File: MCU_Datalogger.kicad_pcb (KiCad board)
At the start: 2 copper layers, 29 parts, among them J1 Conn_01x04_Pin, J2 Conn_01x09_Pin, J3 Conn_01x04_Pin, J4 Conn_02x03_Odd_Even, U1 24LC1025, U2 DS1337S_, U3 24LC1025, U4 ATMEGA328P-AU, Y1 32.768 KHz, Y2 16MHz

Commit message: Completed placement of footprint
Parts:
- moved H3 71.4 mm to (180.7, 59.9)
- moved H4 62.7 mm to (180.7, 85.6)
- moved R7 58.2 mm to (167.8, 63.4)
- moved R5 57.8 mm to (172.3, 63.4)
- moved R6 57.6 mm to (172.3, 66.5)
- moved C5 55.7 mm to (163.0, 60.2)
- moved R4 50.5 mm to (167.7, 66.5)
- moved C3 48.5 mm to (158.4, 60.2)
- moved D2 47.5 mm to (167.7, 60.2)
- moved R3 47.3 mm to (167.8, 69.7), turned to 180 degrees
- moved D1 47.1 mm to (172.4, 60.2)
- moved BT1 46.4 mm to (136.7, 66.7)
- moved U4 42.0 mm to (157.4, 68.7)
- moved C1 41.4 mm to (153.9, 60.2)
- moved C4 40.8 mm to (167.7, 76.7)
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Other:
- board outline added: 50.8 x 30.5 mm

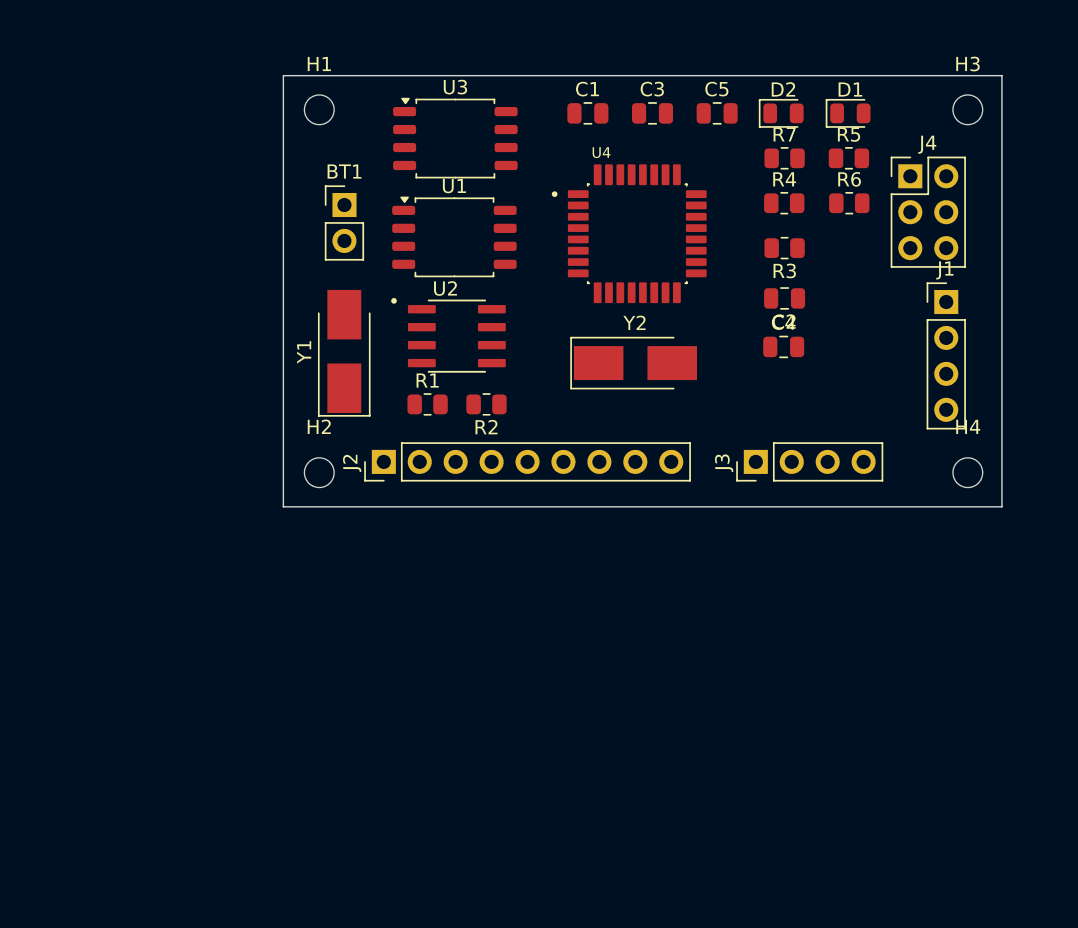
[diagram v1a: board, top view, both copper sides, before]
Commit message: Routing, GND Plane, Rework VCC Line and slick Screen complete
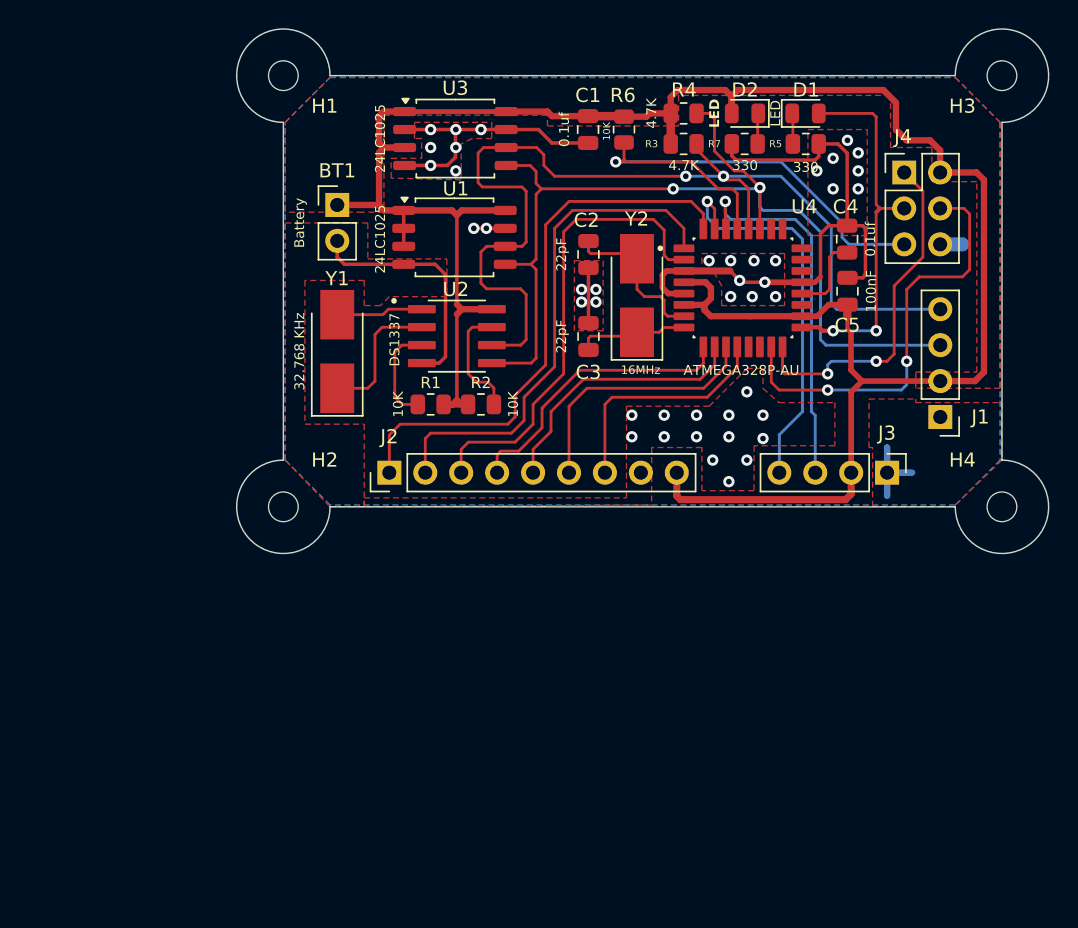
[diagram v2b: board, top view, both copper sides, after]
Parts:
- U2: value DS1337S_ -> DS1337
- moved R6 16.8 mm to (156.4, 61.3), turned to -90 degrees
- moved C3 16.4 mm to (153.9, 76.0), turned to -90 degrees
- moved C5 15.6 mm to (172.2, 72.8), turned to 90 degrees
- moved C2 14.2 mm to (153.9, 70.2), turned to 90 degrees
- moved R3 10.3 mm to (160.6, 62.4), turned to 0 degrees
- moved R4 9.53 mm to (160.6, 60.2)
- moved J3 9.31 mm to (175.0, 85.6), turned to -90 degrees
- moved C4 8.84 mm to (172.2, 69.1), turned to -90 degrees
- moved U4 8.40 mm to (164.8, 72.5)
- moved J1 8.14 mm to (178.8, 81.7), turned to 180 degrees
- moved Y2 4.78 mm to (157.3, 73.1), turned to 90 degrees
- moved H1 3.50 mm to (132.3, 57.5)
- moved H2 3.50 mm to (132.3, 88.0)
- moved H3 3.41 mm to (183.1, 57.5)
- moved H4 3.41 mm to (183.1, 88.0)
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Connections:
- BT1 pad 1: Net-(BT1-+) -> /Vcc
- C5 pad 1: Net-(BT1-+) -> /Vcc
- D1 pad 2: /SCL -> /SCK
- D2 pad 2: Net-(BT1-+) -> /Vcc
- J4 pad 3: /SCL -> /SCK
- U4 pad 17: /SCL -> /SCK
- U4 pad 18: Net-(BT1-+) -> /Vcc
- U4 pad 4: Net-(BT1-+) -> /Vcc
- U4 pad 6: Net-(BT1-+) -> /Vcc
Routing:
- net /Vcc: track 0.00 -> 163.0 mm
- net GND: track 0.00 -> 90.1 mm, vias 0 -> 43
- net /SCL: track 0.00 -> 73.6 mm, vias 0 -> 2
- net /SDA: track 0.00 -> 70.2 mm, vias 0 -> 2
- net /D2: track 0.00 -> 39.8 mm
- net /RESET: track 0.00 -> 36.8 mm, vias 0 -> 1
- net /D3: track 0.00 -> 36.0 mm
- net /D4: track 0.00 -> 33.0 mm
- net /MOSI: track 0.00 -> 30.4 mm, vias 0 -> 2
- net /TX: track 0.00 -> 27.9 mm, vias 0 -> 1
- net /SCK: track 0.00 -> 26.6 mm, vias 0 -> 2
- net /RX: track 0.00 -> 26.6 mm, vias 0 -> 1
- net /MISO: track 0.00 -> 24.9 mm, vias 0 -> 2
- net /D5: track 0.00 -> 20.5 mm
- net /D6: track 0.00 -> 19.0 mm
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- added copper zone on F.Cu, net /Vcc
- added copper zone on B.Cu, net GND
- added copper zone on F.Cu, net GND
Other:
- board size 50.8 x 30.5 mm -> 57.4 x 37.1 mm

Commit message: final 2 layer Layout
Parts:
- added REF**: KiCad-Logo2_5mm_SilkScreen, Symbol:KiCad-Logo2_5mm_SilkScreen, B.Cu at (129.6, 96.7)
- moved H1 25.9 mm to (117.7, 78.9)
- moved R5 25.9 mm to (154.6, 83.7)
- moved C1 25.9 mm to (139.2, 82.7)
- moved D2 25.9 mm to (150.3, 81.6)
- moved BT1 25.9 mm to (121.5, 88.1)
- moved H2 25.9 mm to (117.7, 109.4)
- moved H3 25.9 mm to (168.5, 78.9)
- moved Y1 25.9 mm to (121.5, 98.4)
- moved C2 25.9 mm to (139.2, 91.6)
- moved C3 25.9 mm to (139.2, 97.4)
- moved C4 25.9 mm to (157.5, 90.5)
- moved C5 25.9 mm to (157.5, 94.2)
- moved H4 25.9 mm to (168.5, 109.4)
- moved J1 25.9 mm to (164.1, 103.0)
- moved J2 25.9 mm to (125.1, 107.0)
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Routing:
- net GND: vias 43 -> 39
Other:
- board text added: "+"
- board text added: "0.2000 mm / 0.0000 mm"
- board text added: "0.3000 mm"
- board text added: "1.6000 mm"
- board text added: "2"
- board text added: "3"
- board text added: "4"
- board text added: "5"
- board text added: "57.4079 mm x 37.0879 mm"
- board text added: "6"
- board text added: "7"
- board text added: "8"
- board text added: "BOARD CHARACTERISTICS"
- board text added: "Board Thickness:"
- board text added: "Board overall dimensions:"
- board text added: "Castellated pads:"
- board text added: "Copper Finish:"
- board text added: "Copper Layer Count:"
- board text added: "Designed By: Dhaivat Joshi"
- board text added: "Edge card connectors:"
- board text added: "GND"
- board text added: "GPIO"
- board text added: "I2C"
- board text added: "ICSP"
- board text added: "Impedance Control:"
- board text added: "MISO"
- board text added: "MOSI"
- board text added: "Min hole diameter:"
- board text added: "Min track/spacing:"
- board text added: "No"
- board text added: "None"
- board text added: "Plated Board Edge:"
- board text added: "RST"
- board text added: "RX"
- board text added: "SCK"
- board text added: "SCL"
- board text added: "SDA"
- board text added: "SERIAL"
- board text added: "TX"
- board text added: "V1.2 MCU Datalogger"
- board text added: "VCC"
